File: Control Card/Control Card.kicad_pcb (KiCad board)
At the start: 2 copper layers, 21 parts, among them U1 CY7C1021D, U100 74LS08, U101 74ACT32, U11 74ACT151, U12 74ACT86, U13 74ACT32, U14 74ACT04, U15 74ACT153, U16 74ACT153, U17 74ACT153, U18 74ACT153, U2 CY7C1021D, U20 74ACT02, U21 74ACT20, U24 74ACT30, U3 CY7C1021D, U44 74ACT11, U53 74ACT04, U61 74ACT32

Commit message: add buffers for the write to the µCODE stuff
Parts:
- added U102: 74LVC1G157, Package_SO:SSOP-8_2.95x2.8mm_P0.65mm, F.Cu at (186.1, 106.5)
- added U110: 74ACT244, Package_SO:SOIC-20W_7.5x12.8mm_P1.27mm, F.Cu at (166.1, 156.3)
- added U111: 74ACT374, Package_SO:SOIC-20W_7.5x12.8mm_P1.27mm, F.Cu at (166.4, 99.2)
- added U112: 74ACT374, Package_SO:SOIC-20W_7.5x12.8mm_P1.27mm, F.Cu at (166.2, 112.3)
- added U113: 74ACT374, Package_SO:SOIC-20W_7.5x12.8mm_P1.27mm, F.Cu at (166.2, 126.9)
- U100: value 74LS08 -> 74LVC1G08; footprint Package_SO:SOIC-14_3.9x8.7mm_P1.27mm -> Package_TO_SOT_SMD:SOT-23-5
- U101: value 74ACT32 -> 74LVC1G32; footprint Package_SO:SOIC-14_3.9x8.7mm_P1.27mm -> Package_TO_SOT_SMD:SOT-23-5
- moved J_LEFT1 198.8 mm to (276.3, 190.0), turned to 180 degrees
- moved U12 189.8 mm to (205.3, 123.1)
- moved U11 189.8 mm to (244.5, 105.8)
- moved U15 189.8 mm to (247.2, 143.0)
- moved U16 189.8 mm to (261.7, 100.6)
- moved U17 189.8 mm to (239.5, 84.2)
- moved U18 189.8 mm to (254.7, 86.8)
- moved U20 189.8 mm to (230.6, 124.0)
- moved U21 189.8 mm to (244.6, 124.2)
- moved U24 189.8 mm to (216.7, 123.7)
- moved U44 189.8 mm to (260.7, 125.1)
- moved U53 189.8 mm to (217.7, 140.5)
- moved U61 189.8 mm to (217.9, 106.0)
- moved U13 189.8 mm to (205.3, 103.4)
- moved U14 189.8 mm to (229.4, 105.9)
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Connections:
- net /Microcode/~WR_µCODE~ renamed /Microcode/~RW_µCODE~
- J_LEFT1 pad c24: Net-(J_LEFT1-Padc24) -> DBUS0
- J_LEFT1 pad c25: Net-(J_LEFT1-Padc25) -> DBUS1
- J_LEFT1 pad c26: Net-(J_LEFT1-Padc26) -> DBUS2
- J_LEFT1 pad c27: Net-(J_LEFT1-Padc27) -> DBUS3
- J_LEFT1 pad c28: Net-(J_LEFT1-Padc28) -> DBUS4
- J_LEFT1 pad c29: Net-(J_LEFT1-Padc29) -> DBUS5
- J_LEFT1 pad c30: Net-(J_LEFT1-Padc30) -> DBUS6
- J_LEFT1 pad c31: Net-(J_LEFT1-Padc31) -> DBUS7
- U1 pad 27: /Microcode/SUPERVISOR -> /Microcode/µCODE_SUP
- U100 pad 3: Net-(U100-Pad3) -> GND
- U100 pad 5: Net-(U100-Pad5) -> VCC
- U101 pad 1: Net-(U100-Pad3) -> Net-(U100-Pad4)
- U101 pad 3: /Microcode/µCODE_ADDR_SEL_B -> GND
- U101 pad 4: Net-(U101-Pad4) -> /Microcode/µCODE_ADDR_SEL_B
- U101 pad 5: Net-(U101-Pad5) -> VCC
- U15 pad 10: /Microcode/µCODE_WR_ADDR0 -> /Microcode/µCODE_RW_ADDR0
- U15 pad 6: /Microcode/µCODE_WR_ADDR1 -> /Microcode/µCODE_RW_ADDR1
- U16 pad 10: /Microcode/µCODE_WR_ADDR2 -> /Microcode/µCODE_RW_ADDR2
- U16 pad 6: /Microcode/µCODE_WR_ADDR3 -> /Microcode/µCODE_RW_ADDR3
- U17 pad 10: /Microcode/µCODE_WR_ADDR4 -> /Microcode/µCODE_RW_ADDR4
- U17 pad 6: /Microcode/µCODE_WR_ADDR5 -> /Microcode/µCODE_RW_ADDR5
- U18 pad 10: /Microcode/µCODE_WR_ADDR6 -> /Microcode/µCODE_RW_ADDR6
- U18 pad 6: /Microcode/µCODE_WR_ADDR7 -> /Microcode/µCODE_RW_ADDR7
- U2 pad 27: /Microcode/SUPERVISOR -> /Microcode/µCODE_SUP
- U3 pad 27: /Microcode/SUPERVISOR -> /Microcode/µCODE_SUP

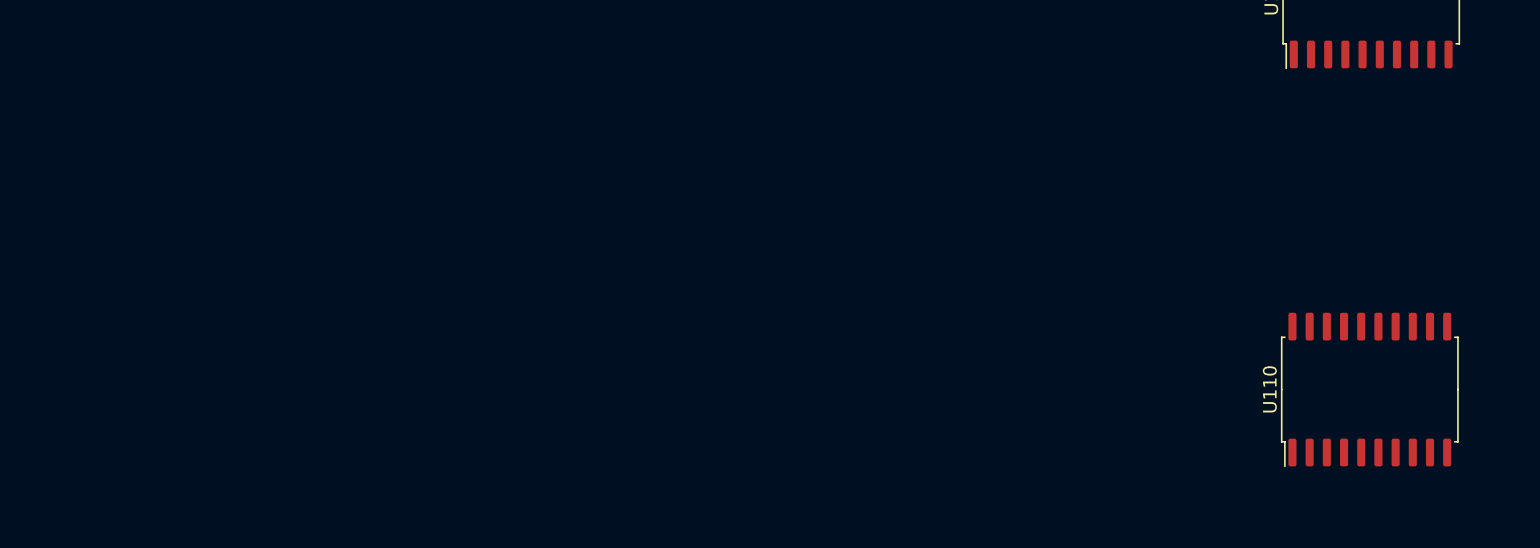
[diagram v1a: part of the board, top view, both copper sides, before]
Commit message: add the µcode output registers
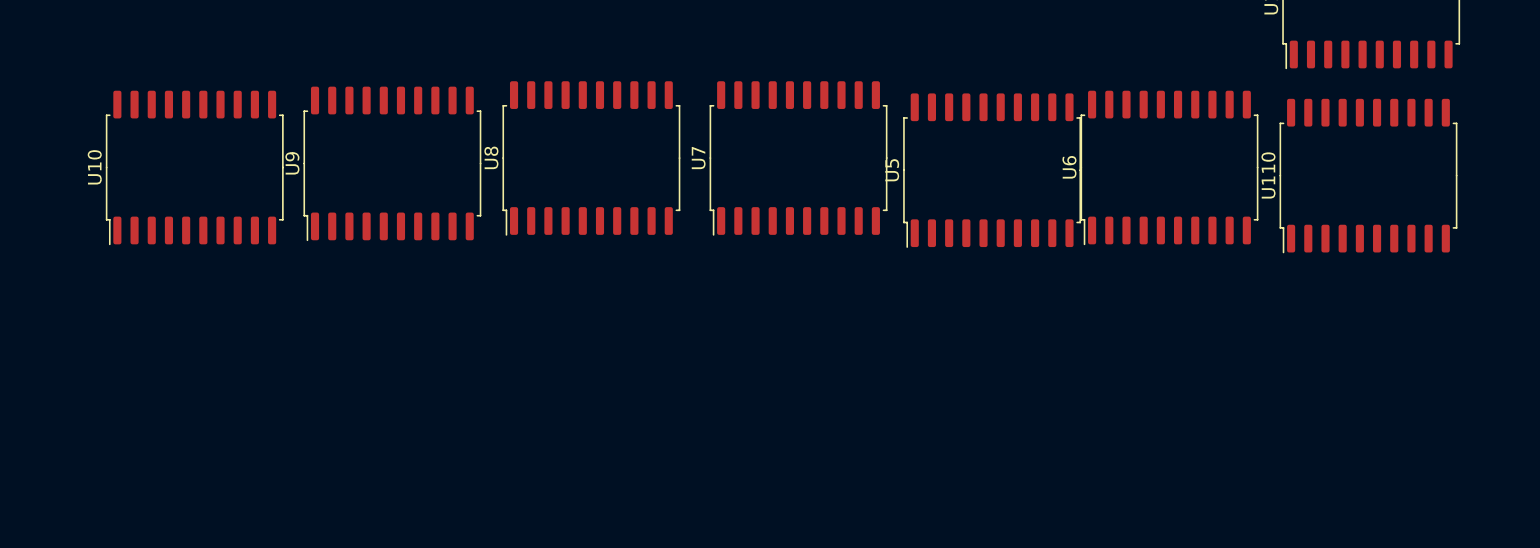
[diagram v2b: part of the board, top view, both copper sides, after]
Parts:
- added U10: 74ACT273, Package_SO:SOIC-20W_7.5x12.8mm_P1.27mm, F.Cu at (79.3, 139.9)
- added U5: 74ACT273, Package_SO:SOIC-20W_7.5x12.8mm_P1.27mm, F.Cu at (138.2, 140.1)
- added U6: 74ACT273, Package_SO:SOIC-20W_7.5x12.8mm_P1.27mm, F.Cu at (151.3, 139.9)
- added U7: 74ACT273, Package_SO:SOIC-20W_7.5x12.8mm_P1.27mm, F.Cu at (123.9, 139.2)
- added U8: 74ACT273, Package_SO:SOIC-20W_7.5x12.8mm_P1.27mm, F.Cu at (108.6, 139.2)
- added U9: 74ACT273, Package_SO:SOIC-20W_7.5x12.8mm_P1.27mm, F.Cu at (93.9, 139.6)
- U102: value 74LVC1G157 -> 74LVC2G157
- moved U110 15.8 mm to (166.0, 140.5)
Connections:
- U1 pad 10: /Microcode/NEXT4 -> /Microcode/io_NEXT4
- U1 pad 13: /Microcode/NEXT3 -> /Microcode/io_NEXT3
- U1 pad 14: /Microcode/NEXT2 -> /Microcode/io_NEXT2
- U1 pad 15: /Microcode/NEXT1 -> /Microcode/io_NEXT1
- U1 pad 16: /Microcode/NEXT0 -> /Microcode/io_NEXT0
- U1 pad 7: /Microcode/NEXT7 -> /Microcode/io_NEXT7
- U1 pad 8: /Microcode/NEXT6 -> /Microcode/io_NEXT6
- U1 pad 9: /Microcode/NEXT5 -> /Microcode/io_NEXT5
- U2 pad 10: /Microcode/LATCH0 -> /Microcode/io_LATCH0
- U2 pad 13: /Microcode/XL_MAR -> /Microcode/io_XL_MAR
- U2 pad 14: /Microcode/XL_MDR_LO -> /Microcode/io_XL_MDR_LO
- U2 pad 15: /Microcode/XL_MDR_HI -> /Microcode/io_XL_MDR_HI
- U2 pad 16: /Microcode/E_MDR_LO -> /Microcode/io_E_MDR_LO
- U2 pad 29: /Microcode/E_MDR_HI -> /Microcode/io_E_MDR_HI
- U2 pad 30: /Microcode/PRIV -> /Microcode/io_PRIV
- U2 pad 31: /Microcode/XL_MODE -> /Microcode/io_XL_MODE
- U2 pad 32: /Microcode/XL_PAGING -> /Microcode/io_XL_PAGING
- U2 pad 35: /Microcode/MISC3 -> /Microcode/io_MISC3
- U2 pad 36: /Microcode/MISC2 -> /Microcode/io_MISC2
- U2 pad 37: /Microcode/MISC1 -> /Microcode/io_MISC1
- U2 pad 38: /Microcode/MISC0 -> /Microcode/io_MISC0
- U2 pad 7: /Microcode/LATCH3 -> /Microcode/io_LATCH3
- U2 pad 8: /Microcode/LATCH2 -> /Microcode/io_LATCH2
- U2 pad 9: /Microcode/LATCH1 -> /Microcode/io_LATCH1
- U3 pad 10: /Microcode/EL0 -> /Microcode/io_EL0
- U3 pad 13: /Microcode/ER1 -> /Microcode/io_ER1
- U3 pad 14: /Microcode/ER0 -> /Microcode/io_ER0
- U3 pad 15: /Microcode/RIMMVAL1 -> /Microcode/io_RIMMVAL1
- U3 pad 16: /Microcode/RIMMVAL0 -> /Microcode/io_RIMMVAL0
- U3 pad 29: /Microcode/ALUOP_SZ -> /Microcode/io_ALUOP_SZ
- U3 pad 30: /Microcode/ALUOP1 -> /Microcode/io_ALUOP1
- U3 pad 31: /Microcode/ALUOP0 -> /Microcode/io_ALUOP0
- U3 pad 32: /Microcode/USE_CARRY -> /Microcode/io_USE_CARRY
- U3 pad 35: /Microcode/LATCH_SZ -> /Microcode/io_LATCH_SZ
- U3 pad 36: /Microcode/NEGATE_BR -> /Microcode/io_NEGATE_BR
- U3 pad 37: /Microcode/RUSER_PTB -> /Microcode/io_RUSER_PTB
- U3 pad 38: /Microcode/CODE_PTB -> /Microcode/io_CODE_PTB
- U3 pad 7: /Microcode/EL3 -> /Microcode/io_EL3
- U3 pad 8: /Microcode/EL2 -> /Microcode/io_EL2
- U3 pad 9: /Microcode/EL1 -> /Microcode/io_EL1

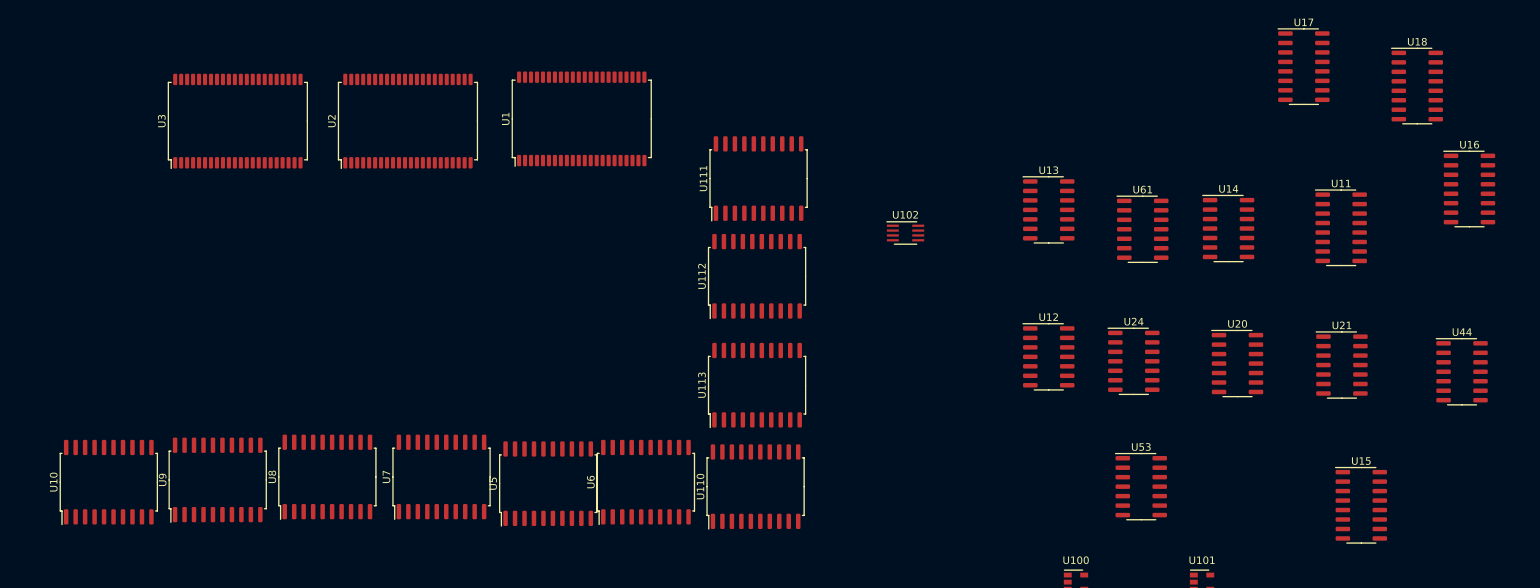
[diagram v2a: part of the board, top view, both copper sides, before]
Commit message: add the µcode data write registers
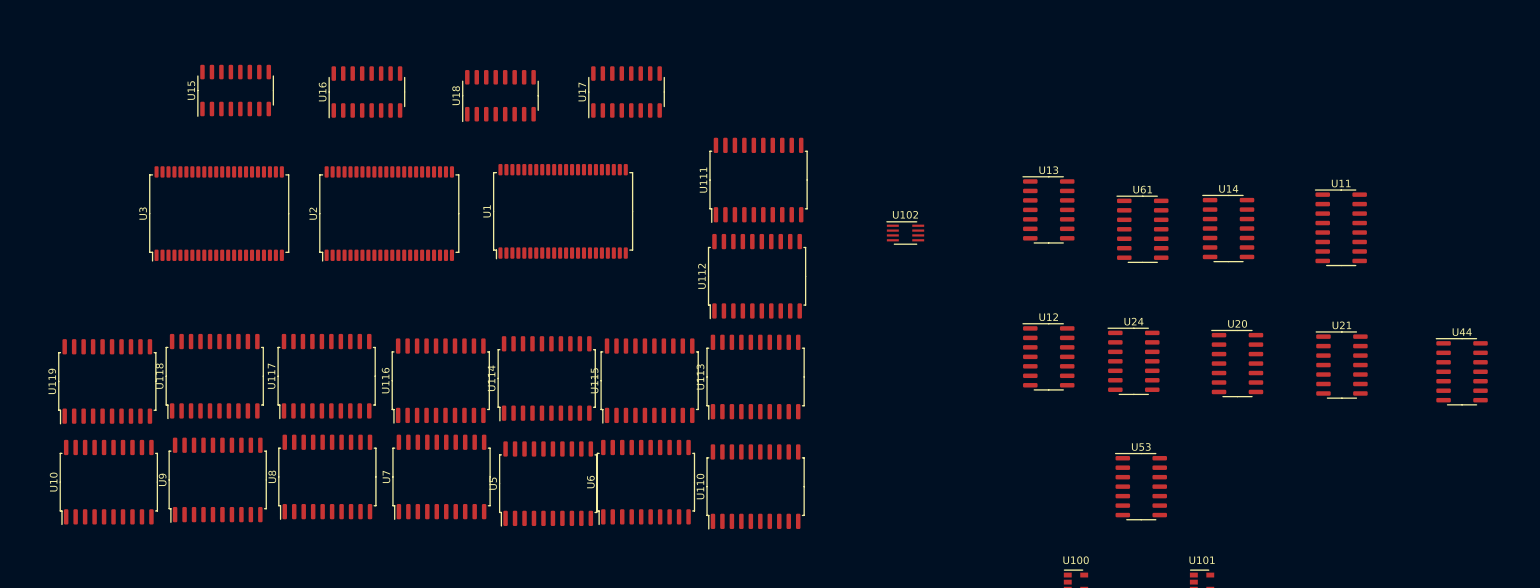
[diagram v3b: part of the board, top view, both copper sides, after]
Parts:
- added U114: 74ACT374, Package_SO:SOIC-20W_7.5x12.8mm_P1.27mm, F.Cu at (138.0, 126.0)
- added U115: 74ACT374, Package_SO:SOIC-20W_7.5x12.8mm_P1.27mm, F.Cu at (151.8, 126.3)
- added U116: 74ACT374, Package_SO:SOIC-20W_7.5x12.8mm_P1.27mm, F.Cu at (123.8, 126.3)
- added U117: 74ACT374, Package_SO:SOIC-20W_7.5x12.8mm_P1.27mm, F.Cu at (108.5, 125.7)
- added U118: 74ACT374, Package_SO:SOIC-20W_7.5x12.8mm_P1.27mm, F.Cu at (93.5, 125.7)
- added U119: 74ACT374, Package_SO:SOIC-20W_7.5x12.8mm_P1.27mm, F.Cu at (79.1, 126.4)
- moved U15 160.8 mm to (96.3, 87.4), turned to 90 degrees
- moved U16 148.4 mm to (113.9, 87.6), turned to 90 degrees
- moved U18 122.9 mm to (131.8, 88.1), turned to 90 degrees
- moved U17 90.9 mm to (148.7, 87.6), turned to 90 degrees
- moved U2 12.6 mm to (116.9, 103.9)
- moved U3 12.6 mm to (94.1, 103.9)
- moved U1 12.6 mm to (140.2, 103.6)
- moved U113 1.12 mm to (166.0, 125.8)
- moved U111 0.20 mm to (166.4, 99.4)

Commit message: add board cutlines
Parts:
- moved U102 102.5 mm to (85.2, 88.5), turned to 90 degrees
- moved U53 34.1 mm to (183.6, 140.7)
- moved U101 32.7 mm to (193.8, 146.6)
- moved J_LEFT1 22.6 mm to (256.0, 180.0)
- moved U100 20.4 mm to (194.0, 139.4)
- moved J_RIGHT1 14.4 mm to (121.0, 180.0)
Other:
- board outline added: 233 x 160 mm
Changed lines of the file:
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@@
   )
   (module "Package_TO_SOT_SMD:SOT-23-5" (layer "F.Cu")
-    (at 225.85 153.3)
+    (at 193.8 146.6)
     (descr "5-pin SOT23 package")
     (tags "SOT-23-5")
@@
   )
   (module "Package_SO:SOIC-14_3.9x8.7mm_P1.27mm" (layer "F.Cu")
-    (at 217.7 140.5)
+    (at 183.6 140.7)
     (descr "SOIC, 14 Pin (JEDEC MS-012AB, https://www.analog.com/media/en/package-pcb-resources/package/pkg_pdf/soic_narrow-r/r_14.pdf), generated with kicad-footprint-generator ipc_gullwing_generator.py")
     (tags "SOIC SO")
@@
   )
   (module "Connector_DIN:DIN41612_C_3x32_Male_Horizontal_THT" (layer "F.Cu")
-    (at 131.6 189.8 180)
+    (at 121 180 180)
     (descr "DIN41612 connector, type C, Horizontal, 3 rows 32 pins wide, https://www.erni-x-press.com/de/downloads/kataloge/englische_kataloge/erni-din41612-iec60603-2-e.pdf")
     (tags "DIN 41612 IEC 60603 C")
@@
   )
   (module "Package_SO:SSOP-8_2.95x2.8mm_P0.65mm" (layer "F.Cu")
-    (at 186.1 106.5)
+    (at 85.2 88.5 90)
     (descr "SSOP-8 2.9 x2.8mm Pitch 0.65mm")
     (tags "SSOP-8 2.95x2.8mm Pitch 0.65mm")
@@
     (property "Sheet name" "Microcode")
     (attr smd)
-    (fp_text reference "U102" (at 0 -2.4) (layer "F.SilkS")
-      (effects (font (size 1 1) (thickness 0.15)))
-    )
-    (fp_text value "74LVC2G157" (at 0 2.6) (layer "F.Fab")
-      (effects (font (size 1 1) (thickness 0.15)))
-    )
-    (fp_text user "${REFERENCE}" (at 0 0) (layer "F.Fab")
+    (fp_text reference "U102" (at 0 -2.4 90) (layer "F.SilkS")
+      (effects (font (size 1 1) (thickness 0.15)))
+    )
+    (fp_text value "74LVC2G157" (at 0 2.6 90) (layer "F.Fab")
+      (effects (font (size 1 1) (thickness 0.15)))
+    )
+    (fp_text user "${REFERENCE}" (at 0 0 90) (layer "F.Fab")
       (effects (font (size 0.6 0.6) (thickness 0.15)))
     )
@@
     (fp_line (start 1.475 -1.4) (end 1.475 1.4) (layer "F.Fab") (width 0.1))
     (fp_line (start -1.475 1.4) (end -1.475 -0.7) (layer "F.Fab") (width 0.1))
-    (pad "1" smd rect (at -1.7 -0.975 270) (size 0.3 1.6) (layers "F.Cu" "F.Paste" "F.Mask")
+    (pad "1" smd rect (at -1.7 -0.975) (size 0.3 1.6) (layers "F.Cu" "F.Paste" "F.Mask")
       (net 204 "/Microcode/SUPERVISOR") (pinfunction "A"))
-    (pad "2" smd rect (at -1.7 -0.325 270) (size 0.3 1.6) (layers "F.Cu" "F.Paste" "F.Mask")
+    (pad "2" smd rect (at -1.7 -0.325) (size 0.3 1.6) (layers "F.Cu" "F.Paste" "F.Mask")
       (net 372 "/Microcode/µCODE_RW_SUP") (pinfunction "B"))
-    (pad "3" smd rect (at -1.7 0.325 270) (size 0.3 1.6) (layers "F.Cu" "F.Paste" "F.Mask")
+    (pad "3" smd rect (at -1.7 0.325) (size 0.3 1.6) (layers "F.Cu" "F.Paste" "F.Mask")
       (net 371 "Net-(U102-Pad3)") (pinfunction "~Y"))
-    (pad "4" smd rect (at -1.7 0.975 270) (size 0.3 1.6) (layers "F.Cu" "F.Paste" "F.Mask")
+    (pad "4" smd rect (at -1.7 0.975) (size 0.3 1.6) (layers "F.Cu" "F.Paste" "F.Mask")
       (net 266 "GND") (pinfunction "GND"))
-    (pad "5" smd rect (at 1.7 0.975 270) (size 0.3 1.6) (layers "F.Cu" "F.Paste" "F.Mask")
+    (pad "5" smd rect (at 1.7 0.975) (size 0.3 1.6) (layers "F.Cu" "F.Paste" "F.Mask")
       (net 369 "/Microcode/µCODE_SUP") (pinfunction "Y"))
-    (pad "6" smd rect (at 1.7 0.325 270) (size 0.3 1.6) (layers "F.Cu" "F.Paste" "F.Mask")
+    (pad "6" smd rect (at 1.7 0.325) (size 0.3 1.6) (layers "F.Cu" "F.Paste" "F.Mask")
       (net 370 "/Microcode/RW_µCODE") (pinfunction "~A~/B"))
-    (pad "7" smd rect (at 1.7 -0.325 270) (size 0.3 1.6) (layers "F.Cu" "F.Paste" "F.Mask")
+    (pad "7" smd rect (at 1.7 -0.325) (size 0.3 1.6) (layers "F.Cu" "F.Paste" "F.Mask")
       (net 266 "GND") (pinfunction "~G"))
-    (pad "8" smd rect (at 1.7 -0.975 270) (size 0.3 1.6) (layers "F.Cu" "F.Paste" "F.Mask")
+    (pad "8" smd rect (at 1.7 -0.975) (size 0.3 1.6) (layers "F.Cu" "F.Paste" "F.Mask")
       (net 267 "VCC") (pinfunction "VCC"))
     (model "${KISYS3DMOD}/Package_SO.3dshapes/SSOP-8_2.95x2.8mm_P0.65mm.wrl"
@@
   )
   (module "Package_TO_SOT_SMD:SOT-23-5" (layer "F.Cu")
-    (at 208.95 153.3)
+    (at 194 139.4)
     (descr "5-pin SOT23 package")
     (tags "SOT-23-5")
@@
   )
   (module "Connector_DIN:DIN41612_C_3x32_Male_Horizontal_THT" (layer "F.Cu")
-    (at 276.3 190 180)
+    (at 256 180 180)
     (descr "DIN41612 connector, type C, Horizontal, 3 rows 32 pins wide, https://www.erni-x-press.com/de/downloads/kataloge/englische_kataloge/erni-din41612-iec60603-2-e.pdf")
     (tags "DIN 41612 IEC 60603 C")
@@
     )
   )
+  (gr_line (start 265 25) (end 265 185) (layer "Edge.Cuts") (width 0.1))
+  (gr_line (start 265 185) (end 32 185) (layer "Edge.Cuts") (width 0.1))
+  (gr_line (start 32 25) (end 265 25) (layer "Edge.Cuts") (width 0.1))
+  (gr_line (start 32 185) (end 32 25) (layer "Edge.Cuts") (width 0.1))
 )

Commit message: connect the enable lines for the µcode rams
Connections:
- U1 pad 17: Net-(U1-Pad17) -> /Microcode/~µCODE_WR~
- U1 pad 39: Net-(U1-Pad39) -> /Microcode/~µCODE_RD~
- U1 pad 40: Net-(U1-Pad40) -> /Microcode/~µCODE_RD~
- U1 pad 41: Net-(U1-Pad41) -> /Microcode/~µCODE_RD~
- U1 pad 6: Net-(U1-Pad6) -> GND
- U2 pad 17: Net-(U2-Pad17) -> /Microcode/~µCODE_WR~
- U2 pad 39: Net-(U2-Pad39) -> /Microcode/~µCODE_RD~
- U2 pad 40: Net-(U2-Pad40) -> /Microcode/~µCODE_RD~
- U2 pad 41: Net-(U2-Pad41) -> /Microcode/~µCODE_RD~
- U2 pad 6: Net-(U2-Pad6) -> GND
- U3 pad 17: Net-(U3-Pad17) -> /Microcode/~µCODE_WR~
- U3 pad 39: Net-(U3-Pad39) -> /Microcode/~µCODE_RD~
- U3 pad 40: Net-(U3-Pad40) -> /Microcode/~µCODE_RD~
- U3 pad 41: Net-(U3-Pad41) -> /Microcode/~µCODE_RD~
- U3 pad 6: Net-(U3-Pad6) -> GND

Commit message: some updates to the PCB (no idea what)
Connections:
- net Net-(U5-Pad12) renamed /Microcode/µCODE_WR_PRIME
- net Net-(U5-Pad15) renamed /Microcode/µCODE_L_RUN_PAGE
- net Net-(U5-Pad2) renamed /Microcode/µCODE_REGISTERS2
- net Net-(U5-Pad5) renamed /Microcode/µCODE_REGISTERS1
- net Net-(U5-Pad6) renamed /Microcode/µCODE_REGISTERS0
- net Net-(U5-Pad9) renamed /Microcode/µCODE_L_REGISTERS
- U1 pad 29: Net-(U1-Pad29) -> /Microcode/io_µCODE_REGISTERS2
- U1 pad 30: Net-(U1-Pad30) -> /Microcode/io_µCODE_REGISTERS1
- U1 pad 31: Net-(U1-Pad31) -> /Microcode/io_µCODE_REGISTERS0
- U1 pad 32: Net-(U1-Pad32) -> /Microcode/io_µCODE_L_REGISTERS
- U1 pad 35: Net-(U1-Pad35) -> /Microcode/io_µCODE_WR_PRIME
- U1 pad 36: Net-(U1-Pad36) -> /Microcode/io_µCODE_L_RUN_PAGE
- U114 pad 12: Net-(U114-Pad12) -> /Microcode/io_µCODE_WR_PRIME
- U114 pad 15: Net-(U114-Pad15) -> /Microcode/io_µCODE_L_RUN_PAGE
- U114 pad 2: Net-(U114-Pad2) -> /Microcode/io_µCODE_REGISTERS2
- U114 pad 5: Net-(U114-Pad5) -> /Microcode/io_µCODE_REGISTERS1
- U114 pad 6: Net-(U114-Pad6) -> /Microcode/io_µCODE_REGISTERS0
- U114 pad 9: Net-(U114-Pad9) -> /Microcode/io_µCODE_L_REGISTERS
- U5 pad 13: Net-(U5-Pad13) -> /Microcode/io_µCODE_WR_PRIME
- U5 pad 14: Net-(U5-Pad14) -> /Microcode/io_µCODE_L_RUN_PAGE
- U5 pad 3: Net-(U5-Pad3) -> /Microcode/io_µCODE_REGISTERS2
- U5 pad 4: Net-(U5-Pad4) -> /Microcode/io_µCODE_REGISTERS1
- U5 pad 7: Net-(U5-Pad7) -> /Microcode/io_µCODE_REGISTERS0
- U5 pad 8: Net-(U5-Pad8) -> /Microcode/io_µCODE_L_REGISTERS
